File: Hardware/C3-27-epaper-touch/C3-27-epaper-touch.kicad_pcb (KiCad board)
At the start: 4 copper layers, 65.4 x 71 mm, 62 parts, among them J1 AFC24-S24FIC-00, J2 USB_C_Programming, J3 Conn_01x06, J4 Conn_01x06_Female, J5 Groove sensor, Q1 Si1308, Q2 BC817, Q3 BC817, U1 ESP32-C3-WROOM-02-N4, U2 CP2102N-A02-GQFN28R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

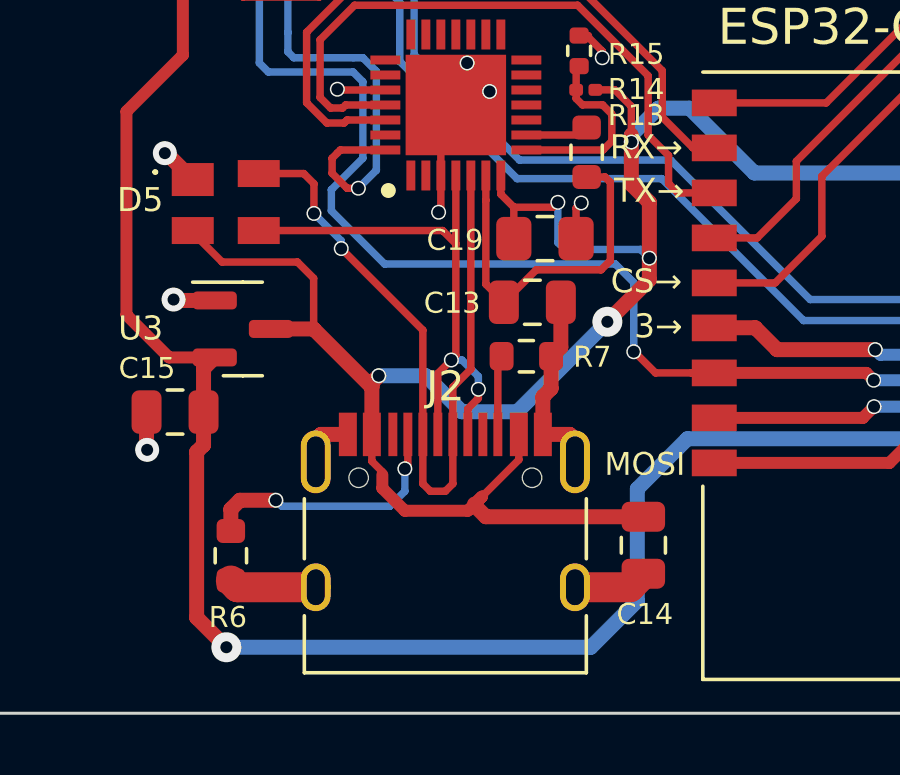
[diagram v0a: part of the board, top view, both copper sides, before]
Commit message: Update C15 put it closer to LDO
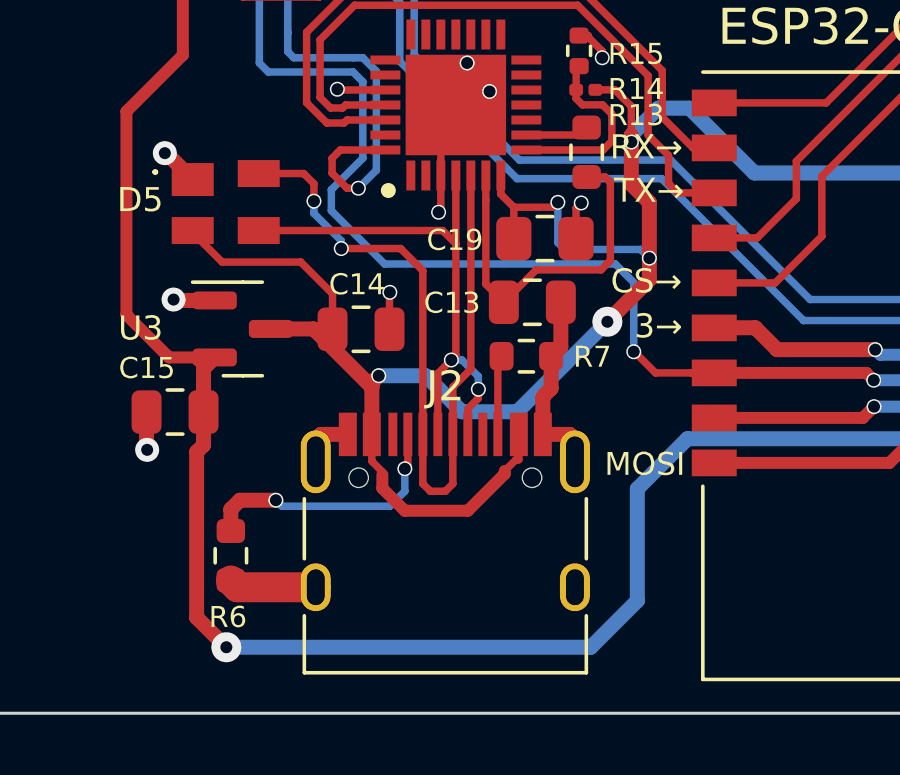
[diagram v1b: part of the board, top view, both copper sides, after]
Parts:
- moved C14 11.8 mm to (122.0, 113.2), turned to 0 degrees
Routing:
- net VBUS: track 109.2 -> 103.2 mm
- net GND: track 78.0 -> 76.7 mm, vias 30 -> 31
- net Net-(D5-Pad4): track 25.2 -> 26.4 mm

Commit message: C3 Rev 1.1 sent to fabrication
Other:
- board size 65.4 x 71 mm -> 70.2 x 71 mm
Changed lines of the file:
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@@
     (property "Sheetfile" "C3-27-epaper-touch.kicad_sch")
     (property "Sheetname" "")
-    (attr through_hole exclude_from_pos_files)
+    (attr through_hole)
     (fp_text reference "U1" (at -2.366 11.62) (layer "F.SilkS")
       (effects (font (size 1.2 1.2) (thickness 0.15)))
@@
     (property "Sheetfile" "C3-27-epaper-touch.kicad_sch")
     (property "Sheetname" "")
-    (attr through_hole exclude_from_pos_files)
+    (attr through_hole exclude_from_pos_files exclude_from_bom)
     (fp_text reference "J5" (at -2.95 1.67) (layer "F.SilkS")
       (effects (font (size 0.9 0.9) (thickness 0.14)))
@@
   (gr_line (start 117.35 56.65) (end 117.35 56.2) (layer "F.SilkS") (width 0.15))
   (gr_line (start 152.65 72.5) (end 152.65 57.5) (layer "F.SilkS") (width 0.15))
+  (gr_line (start 170.65 126) (end 170.65 94) (layer "Edge.Cuts") (width 0.1))
+  (gr_line (start 170.65 55) (end 175 55) (layer "Edge.Cuts") (width 0.1))
+  (gr_line (start 170.2 94) (end 170.65 94) (layer "Edge.Cuts") (width 0.1))
   (gr_line (start 117.2 55) (end 104.8 55) (layer "Edge.Cuts") (width 0.1))
   (gr_line (start 142.82 55) (end 170.2 55) (layer "Edge.Cuts") (width 0.1))
   (gr_line (start 117.2 55.8) (end 142.82 55.8) (layer "Edge.Cuts") (width 0.1))
   (gr_line (start 104.8 126) (end 170.2 126) (layer "Edge.Cuts") (width 0.1))
-  (gr_line (start 170.2 126) (end 170.2 55) (layer "Edge.Cuts") (width 0.1))
+  (gr_line (start 170.2 86) (end 170.2 55) (layer "Edge.Cuts") (width 0.1))
   (gr_line (start 104.8 55) (end 104.8 126) (layer "Edge.Cuts") (width 0.1))
+  (gr_line (start 175 126) (end 170.65 126) (layer "Edge.Cuts") (width 0.1))
+  (gr_line (start 175 126) (end 175 55) (layer "Edge.Cuts") (width 0.1))
   (gr_line (start 142.82 55.8) (end 142.82 55) (layer "Edge.Cuts") (width 0.1))
+  (gr_line (start 170.2 126) (end 170.2 94) (layer "Edge.Cuts") (width 0.1))
+  (gr_line (start 170.2 86) (end 170.65 86) (layer "Edge.Cuts") (width 0.1))
+  (gr_line (start 170.65 86) (end 170.65 55) (layer "Edge.Cuts") (width 0.1))
   (gr_line (start 117.2 55) (end 117.2 55.8) (layer "Edge.Cuts") (width 0.1))
   (gr_text "GND" (at 154.8 102.4) (layer "B.SilkS")

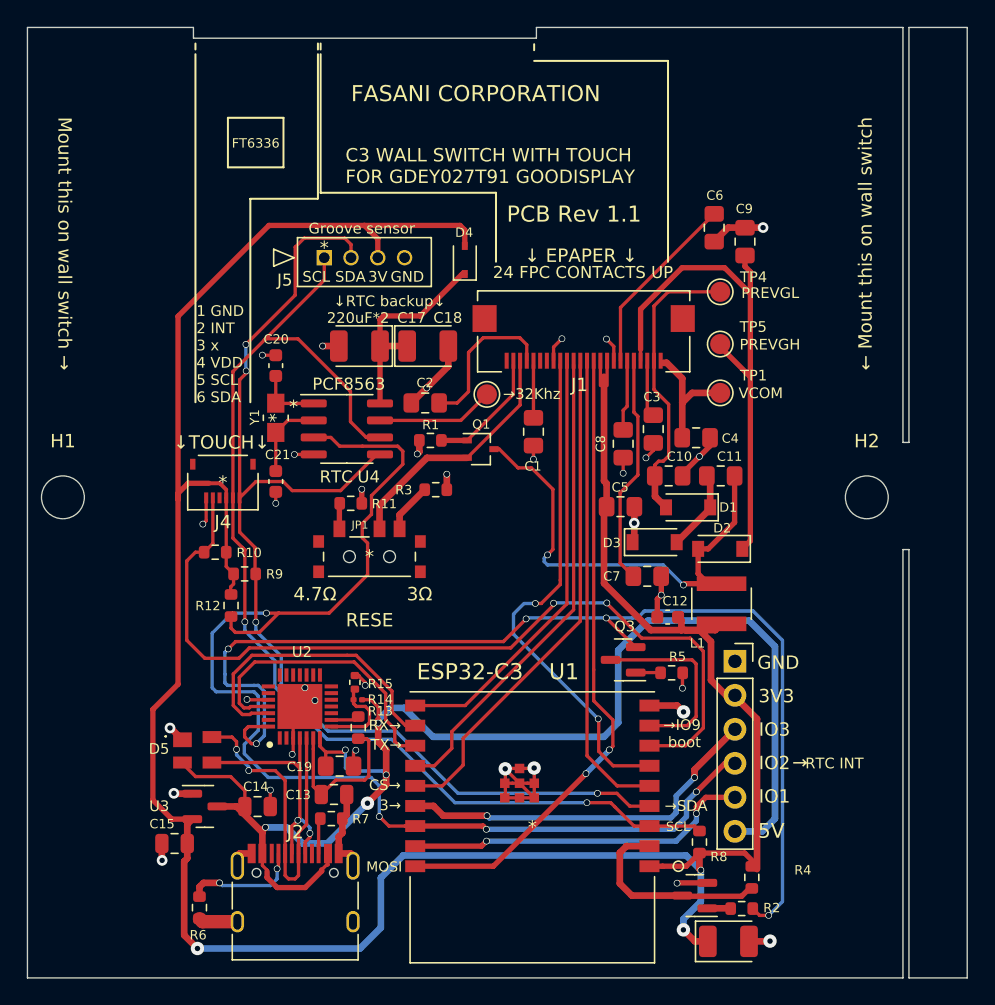
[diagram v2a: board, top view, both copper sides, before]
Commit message: C3 Rev 1.2 start: Simplify routing
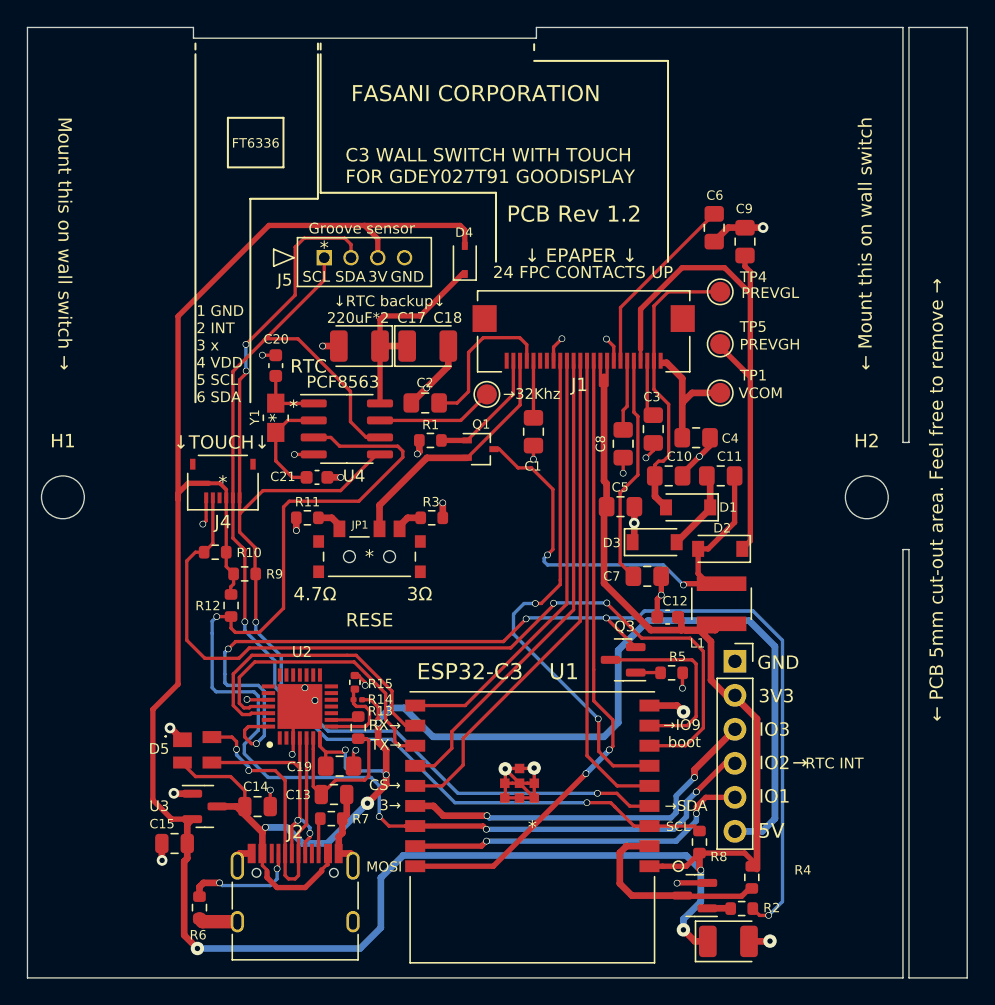
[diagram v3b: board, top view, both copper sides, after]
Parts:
- moved R11 3.42 mm to (125.7, 91.6), turned to 180 degrees
- moved C21 3.10 mm to (126.4, 88.6), turned to 180 degrees
- moved R3 2.12 mm to (135.0, 91.6)
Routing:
- net /IO_2: track 91.8 -> 89.1 mm
- net Net-(C21-Pad2): track 6.09 -> 8.15 mm
- net Net-(JP1-Pad3): track 3.70 -> 1.81 mm
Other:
- board text added: "PCB Rev 1.2"
- board text added: "← PCB 5mm cut-out area. Feel free to remove →"
- board text removed: "PCB Rev 1.1"

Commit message: Mark properly D+ & D- lines
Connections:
- net Net-(D5-Pad3) renamed /D+
- net Net-(D5-Pad4) renamed /D-
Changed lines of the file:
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@@
   (net 69 "unconnected-(U2-Pad27)")
   (net 70 "Net-(R14-Pad1)")
-  (net 71 "Net-(D5-Pad3)")
-  (net 72 "Net-(D5-Pad4)")
+  (net 71 "/D+")
+  (net 72 "/D-")
   (footprint "TestPoint:TestPoint_Pad_D1.5mm" (layer "F.Cu")
     (at 156.55 82.3)
@@
     (property "Sheetfile" "C3-27-epaper-touch.kicad_sch")
     (property "Sheetname" "")
-    (attr exclude_from_pos_files exclude_from_bom)
+    (attr exclude_from_pos_files)
     (fp_text reference "TP1" (at 2.49 -1.3) (layer "F.SilkS")
       (effects (font (size 0.8 0.8) (thickness 0.13)))
@@
     (property "Sheetfile" "C3-27-epaper-touch.kicad_sch")
     (property "Sheetname" "")
-    (attr exclude_from_pos_files exclude_from_bom)
+    (attr exclude_from_pos_files)
     (fp_text reference "TP3" (at 0 -1.648) (layer "F.SilkS") hide
       (effects (font (size 0.8 0.8) (thickness 0.13)))
@@
       (net 37 "Net-(J2-PadA5)") (pinfunction "CC1") (pintype "bidirectional"))
     (pad "A6" smd rect (at -0.25 -4.045) (size 0.3 1.45) (layers "F.Cu" "F.Paste" "F.Mask")
-      (net 71 "Net-(D5-Pad3)") (pinfunction "D+") (pintype "bidirectional"))
+      (net 71 "/D+") (pinfunction "D+") (pintype "bidirectional"))
     (pad "A7" smd rect (at 0.25 -4.045) (size 0.3 1.45) (layers "F.Cu" "F.Paste" "F.Mask")
-      (net 72 "Net-(D5-Pad4)") (pinfunction "D-") (pintype "bidirectional"))
+      (net 72 "/D-") (pinfunction "D-") (pintype "bidirectional"))
     (pad "A8" smd rect (at 1.25 -4.045) (size 0.3 1.45) (layers "F.Cu" "F.Paste" "F.Mask")
       (net 18 "unconnected-(J2-PadA8)") (pinfunction "SBU1") (pintype "bidirectional+no_connect"))
@@
       (net 12 "Net-(J2-PadB5)") (pinfunction "CC2") (pintype "bidirectional"))
     (pad "B6" smd rect (at 0.75 -4.045) (size 0.3 1.45) (layers "F.Cu" "F.Paste" "F.Mask")
-      (net 71 "Net-(D5-Pad3)") (pinfunction "D+") (pintype "bidirectional"))
+      (net 71 "/D+") (pinfunction "D+") (pintype "bidirectional"))
     (pad "B7" smd rect (at -0.75 -4.045) (size 0.3 1.45) (layers "F.Cu" "F.Paste" "F.Mask")
-      (net 72 "Net-(D5-Pad4)") (pinfunction "D-") (pintype "bidirectional"))
+      (net 72 "/D-") (pinfunction "D-") (pintype "bidirectional"))
     (pad "B8" smd rect (at -1.75 -4.045) (size 0.3 1.45) (layers "F.Cu" "F.Paste" "F.Mask")
       (net 38 "unconnected-(J2-PadB8)") (pinfunction "SBU2") (pintype "bidirectional+no_connect"))
@@
     (property "Arrow Price/Stock" "https://www.arrow.com/en/products/sp0503bahtg/littelfuse?region=nac")
     (property "Description" "ESD Suppressors / TVS Diodes TVS AVAL DIODE SMT")
-    (property "Height" "1.22")
+    (property "LCSC" "C3040626")
     (property "Manufacturer_Name" "LITTELFUSE")
     (property "Manufacturer_Part_Number" "SP0503BAHTG")
@@
       (net 3 "VBUS") (pinfunction "K_1") (pintype "passive"))
     (pad "3" smd rect (at 0.95 -1.1 270) (size 0.9 1.4) (layers "F.Cu" "F.Paste" "F.Mask")
-      (net 71 "Net-(D5-Pad3)") (pinfunction "K_2") (pintype "passive"))
+      (net 71 "/D+") (pinfunction "K_2") (pintype "passive"))
     (pad "4" smd rect (at -0.95 -1.1 270) (size 0.9 1.4) (layers "F.Cu" "F.Paste" "F.Mask")
-      (net 72 "Net-(D5-Pad4)") (pinfunction "K_3") (pintype "passive"))
+      (net 72 "/D-") (pinfunction "K_3") (pintype "passive"))
     (model "${KIPRJMOD}/parts/3d/SP0503BAHTG-ESD.step"
       (offset (xyz 0 -0.02999999888 0.6899999873))
@@
     (descr "SOIC, 8 Pin (JEDEC MS-012AA, https://www.analog.com/media/en/package-pcb-resources/package/pkg_pdf/soic_narrow-r/r_8.pdf), generated with kicad-footprint-generator ipc_gullwing_generator.py")
     (tags "SOIC SO")
+    (property "LCSC" "C7440")
     (property "Sheetfile" "C3-27-epaper-touch.kicad_sch")
     (property "Sheetname" "")
@@
     (property "Sheetfile" "C3-27-epaper-touch.kicad_sch")
     (property "Sheetname" "")
-    (attr exclude_from_pos_files exclude_from_bom)
+    (attr exclude_from_pos_files)
     (fp_text reference "TP4" (at 2.49 -1.1) (layer "F.SilkS")
       (effects (font (size 0.8 0.8) (thickness 0.13)))
@@
     (property "Sheetfile" "C3-27-epaper-touch.kicad_sch")
     (property "Sheetname" "")
-    (attr exclude_from_pos_files exclude_from_bom)
+    (attr exclude_from_pos_files)
     (fp_text reference "H1" (at 0 -4.2) (layer "F.SilkS")
       (effects (font (size 1 1) (thickness 0.15)))
@@
       (net 1 "GND") (pinfunction "GND_1") (pintype "passive"))
     (pad "4" smd rect (at -2.35 0 180) (size 0.3 1) (layers "F.Cu" "F.Paste" "F.Mask")
-      (net 71 "Net-(D5-Pad3)") (pinfunction "D+") (pintype "passive"))
+      (net 71 "/D+") (pinfunction "D+") (pintype "passive"))
     (pad "5" smd rect (at -2.35 0.5 180) (size 0.3 1) (layers "F.Cu" "F.Paste" "F.Mask")
-      (net 72 "Net-(D5-Pad4)") (pinfunction "D-") (pintype "passive"))
+      (net 72 "/D-") (pinfunction "D-") (pintype "passive"))
     (pad "6" smd rect (at -2.35 1 180) (size 0.3 1) (layers "F.Cu" "F.Paste" "F.Mask")
       (net 41 "Net-(C13-Pad1)") (pinfunction "VDD") (pintype "passive"))
@@
     (property "Sheetfile" "C3-27-epaper-touch.kicad_sch")
     (property "Sheetname" "")
-    (attr through_hole exclude_from_pos_files exclude_from_bom)
+    (attr through_hole exclude_from_pos_files)
     (fp_text reference "J5" (at -2.95 1.67) (layer "F.SilkS")
       (effects (font (size 0.9 0.9) (thickness 0.14)))
@@
     (property "Sheetfile" "C3-27-epaper-touch.kicad_sch")
     (property "Sheetname" "")
-    (attr through_hole exclude_from_pos_files exclude_from_bom)
+    (attr through_hole exclude_from_pos_files)
     (fp_text reference "J3" (at 3.5 -0.1) (layer "F.SilkS") hide
       (effects (font (size 1 1) (thickness 0.15)))
@@
     (property "Sheetfile" "C3-27-epaper-touch.kicad_sch")
     (property "Sheetname" "")
-    (attr exclude_from_pos_files exclude_from_bom)
+    (attr exclude_from_pos_files)
     (fp_text reference "TP5" (at 2.47 -1.28) (layer "F.SilkS")
       (effects (font (size 0.8 0.8) (thickness 0.13)))
@@
     (property "Sheetfile" "C3-27-epaper-touch.kicad_sch")
     (property "Sheetname" "")
-    (attr exclude_from_pos_files exclude_from_bom)
+    (attr exclude_from_pos_files)
     (fp_text reference "H2" (at 0 -4.2) (layer "F.SilkS")
       (effects (font (size 1 1) (thickness 0.15)))

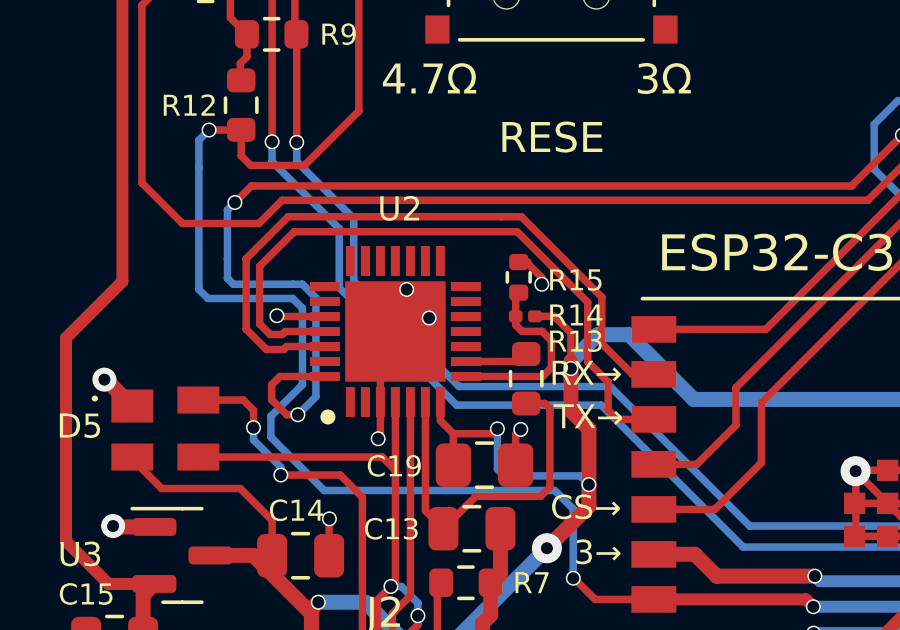
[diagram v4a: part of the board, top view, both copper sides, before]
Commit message: Update 1.1 R14 & R15 VUSB sense CP2102
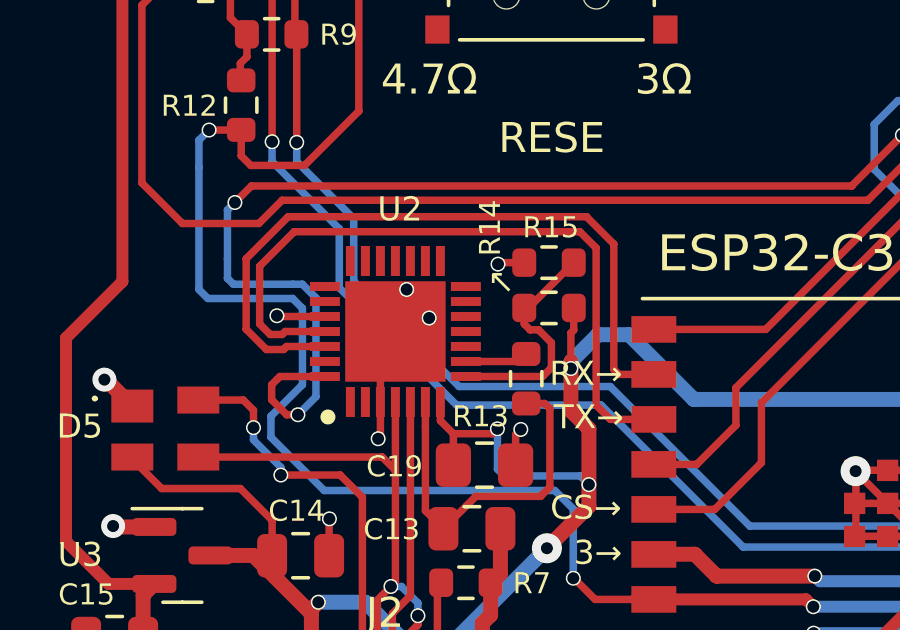
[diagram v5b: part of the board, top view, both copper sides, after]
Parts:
- R14: footprint Resistor_SMD:R_0201_0603Metric -> Resistor_SMD:R_0603_1608Metric
- R15: footprint Resistor_SMD:R_0402_1005Metric -> Resistor_SMD:R_0603_1608Metric
- moved R15 1.12 mm to (130.3, 103.4), turned to 0 degrees
- moved R14 0.84 mm to (130.3, 104.9)
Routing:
- net TX: track 22.5 -> 24.1 mm
- net Net-(R14-Pad1): track 6.40 -> 7.78 mm
- net RX: track 22.2 -> 23.6 mm
- net GND: track 76.8 -> 76.1 mm
- net VBUS: track 103.2 -> 102.6 mm
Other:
- board text added: "↖"

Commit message: C3 1.1 replace C13 to be 4.7uF
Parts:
- C13: value 100nF -> 4.7uF
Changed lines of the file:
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@@
     (descr "Capacitor SMD 0805 (2012 Metric), square (rectangular) end terminal, IPC_7351 nominal, (Body size source: IPC-SM-782 page 76, https://www.pcb-3d.com/wordpress/wp-content/uploads/ipc-sm-782a_amendment_1_and_2.pdf, https://docs.google.com/spreadsheets/d/1BsfQQcO9C6DZCsRaXUlFlo91Tg2WpOkGARC1WS5S8t0/edit?usp=sharing), generated with kicad-footprint-generator")
     (tags "capacitor")
-    (property "LCSC" "C28233")
+    (property "LCSC" "C1779")
     (property "Sheetfile" "C3-27-epaper-touch.kicad_sch")
     (property "Sheetname" "")
@@
       (effects (font (size 0.7 0.7) (thickness 0.13)))
     )
-    (fp_text value "100nF" (at 0 1.68) (layer "F.Fab")
+    (fp_text value "4.7uF" (at 0 1.68) (layer "F.Fab")
       (effects (font (size 1 1) (thickness 0.15)))
     )
